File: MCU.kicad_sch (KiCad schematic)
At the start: 30 parts, among them U4 STM32U595RITx, U8 ATECC608A-SSHDA, X1 SMD3225-4, X2 SMD2012-2

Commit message: WIP: remove unneeded parts from PCB, add SPA06 and FHTC3 to schematics
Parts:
- C25, J_BOOT1, J_RST1, R11, R24, R25, R9, U8: now not fitted; now left out of the parts list
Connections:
- net SAI_FS: now also R25.1, U4.58 (PB6)
- net SAI_MCLK: now also R11.1, U4.56 (PB4)
- net SAI_SCK: now also R9.1, U4.55 (PB3)
- net SAI_SD: now also R24.1, U4.57 (PB5)
- net I2C3_SCL renamed I2C2_SCL
- net I2C3_SDA renamed I2C2_SDA
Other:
- moved on the sheet: R13, R14

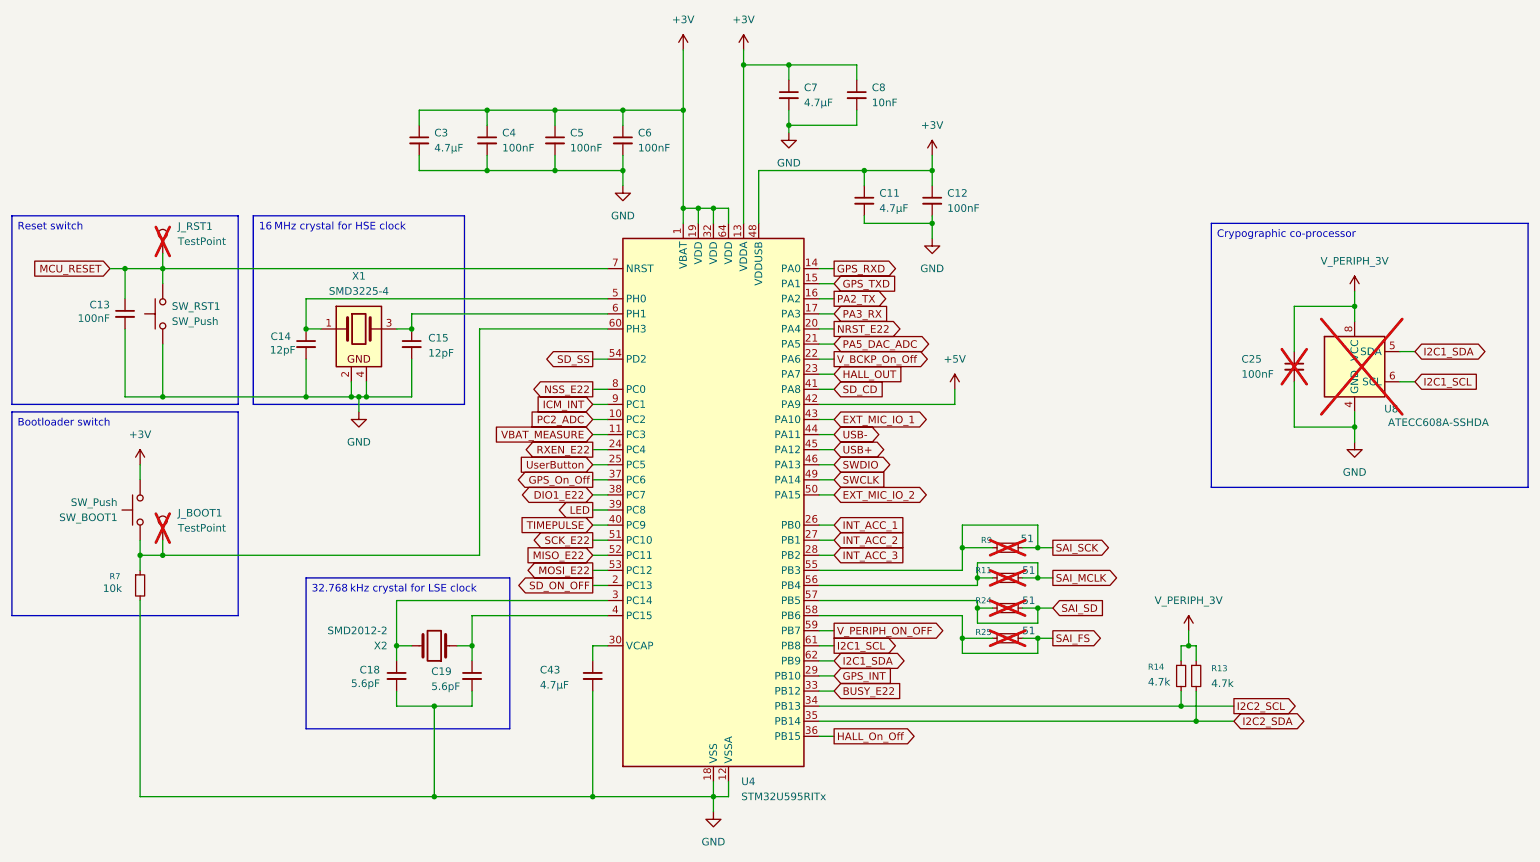
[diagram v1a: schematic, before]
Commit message: WIP: import ambient-pcb-lifepo4protection and ambient-pcb-audiopower schematics
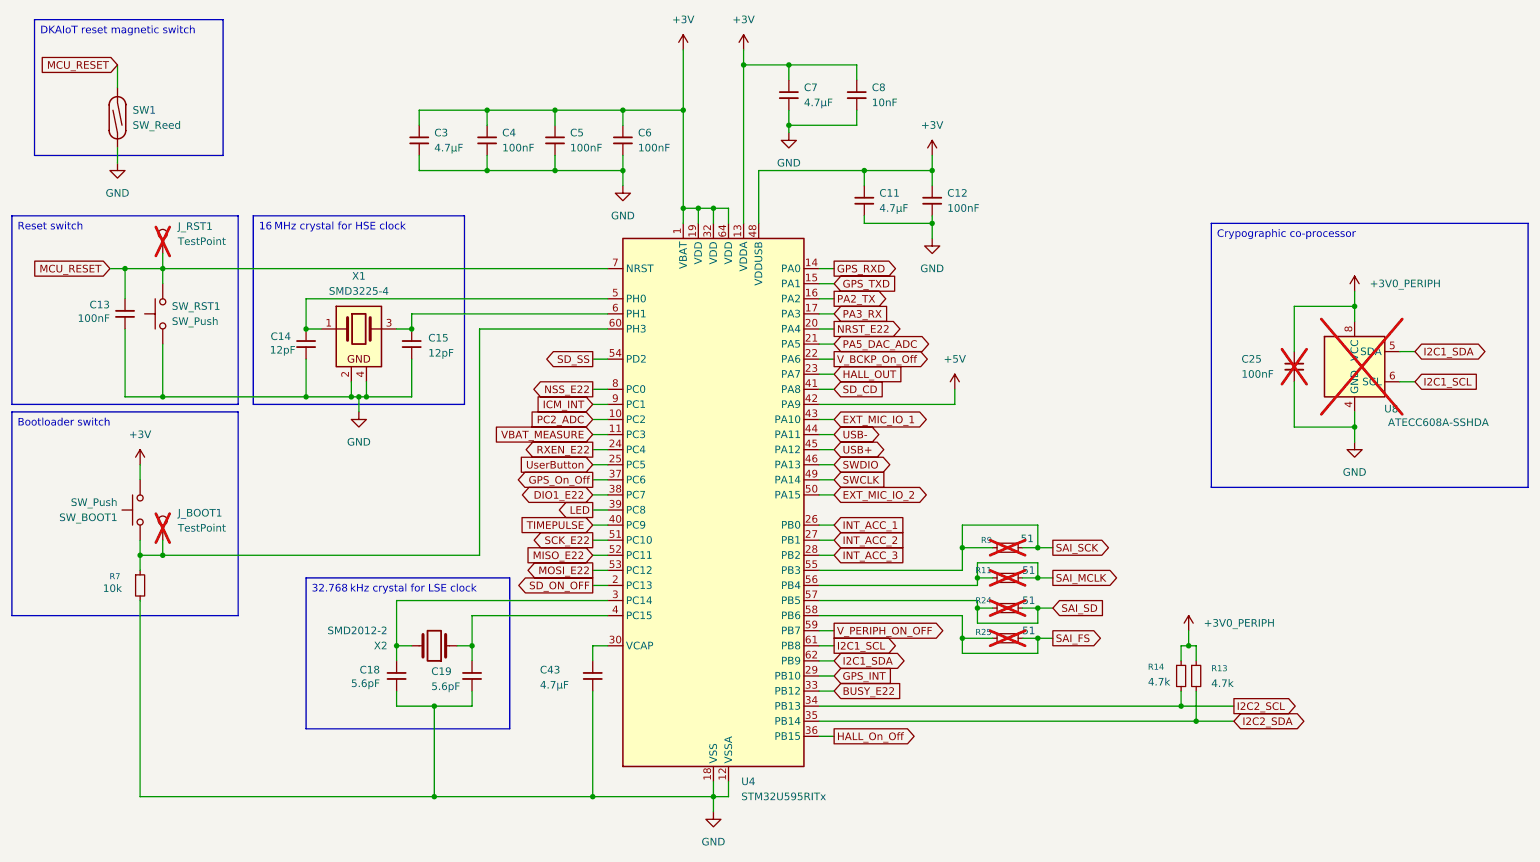
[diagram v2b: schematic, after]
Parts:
- added SW1: SW_Reed, Resistor_THT:R_Axial_DIN0207_L6.3mm_D2.5mm_P10.16mm_Horizontal, symbol Switch:SW_Reed
- C25: now in the parts list
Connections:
- net GND: now also SW1.1
- net MCU_RESET: now also SW1.2
- net V_PERIPH_3V renamed +3V0_PERIPH

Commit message: WIP: BOM
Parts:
- removed X2: SMD2012-2, PCM_Crystal_AKL:Crystal_SMD_2012-2Pin_2.0x1.2mm, symbol PCM_Crystal_AKL:SMD2012-2
- added X2: SMD3215-2 32.768kHz, PCM_Crystal_AKL:Crystal_SMD_3215-2Pin_3.2x1.5mm, symbol PCM_Crystal_AKL:SMD3215-2
- C11, C3, C43, C7: LCSC (none) -> C23733
- C12, C13, C4, C5, C6: LCSC (none) -> C1525
- C14, C15: LCSC (none) -> C1547
- C18, C19: value 5.6pF -> 12pF; LCSC (none) -> C1547
- C25: LCSC (none) -> C1525; now left out of the parts list
- C8: LCSC (none) -> C15195
- R11, R24, R25, R9: value 51 -> 33; LCSC (none) -> C25105
- R13, R14: LCSC (none) -> C25900
- R7: LCSC (none) -> C25744
- SW_BOOT1, SW_RST1: LCSC (none) -> C223812
- U4: LCSC (none) -> C28563722; LCSC Old (none) -> C28247611
- U8: LCSC (none) -> C616024
- X1: LCSC (none) -> C13738
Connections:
- net SD_ON_OFF: now also U4.59 (PB7); no longer U4.2 (PC13)
- net V_PERIPH_ON_OFF: now also U4.2 (PC13); no longer U4.59 (PB7)
- net at C18.1, U4.3 (PC14): now also X2.1
- net at C19.1, U4.4 (PC15): now also X2.2
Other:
- moved on the sheet: C18, C19

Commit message: Finish routing + silkscreen placement
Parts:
- SW_BOOT1, SW_RST1: FT Rotation Offset (none) -> 180
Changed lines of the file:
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@@
+			)
+		)
+		(property "FT Rotation Offset" "180"
+			(at 40.64 63.5 90)
+			(hide yes)
+			(show_name no)
+			(do_not_autoplace no)
+			(effects
+				(font
+					(size 1.27 1.27)
+				)
 			)
 		)
@@
 			(at 36.83 96.52 90)
 			(hide yes)
+			(show_name no)
+			(do_not_autoplace no)
+			(effects
+				(font
+					(size 1.27 1.27)
+				)
+			)
+		)
+		(property "FT Rotation Offset" "180"
+			(at 36.83 96.52 90)
+			(hide yes)
